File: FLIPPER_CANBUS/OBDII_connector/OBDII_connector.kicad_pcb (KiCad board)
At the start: 2 copper layers, 40 x 16.9 mm, 9 parts, among them J1 Conn_02x08_Counter_Clockwise, J2 Conn_01x02

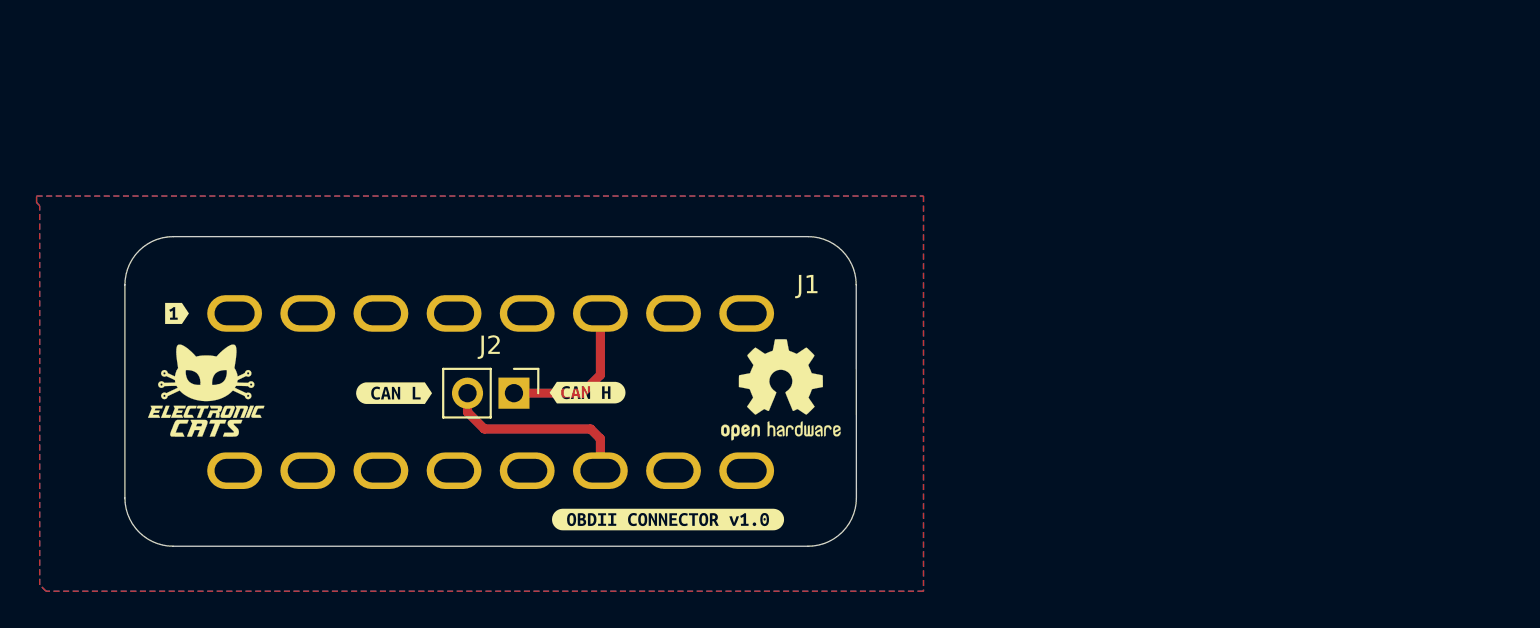
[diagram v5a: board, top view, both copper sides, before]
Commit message: feat: new dimensions added for OBDII connector
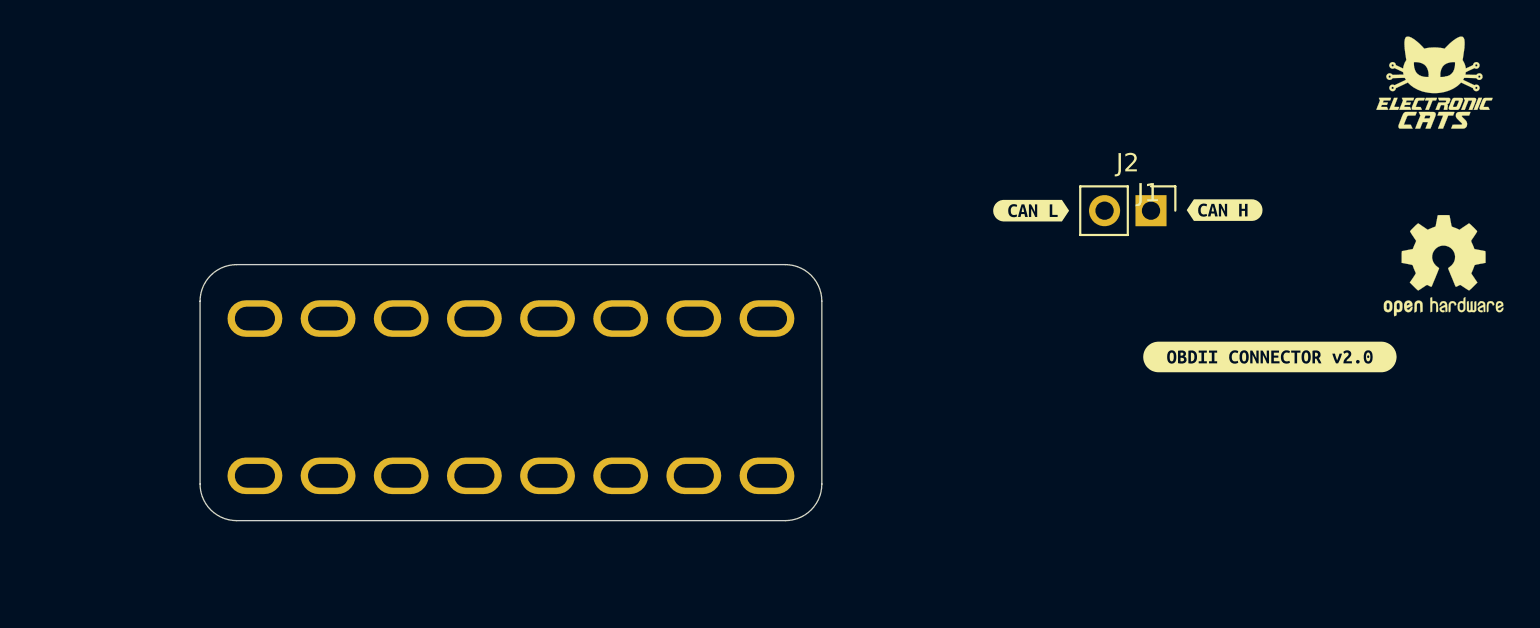
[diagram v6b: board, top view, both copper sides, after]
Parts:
- removed kibuzzard-66732750: G***, kibuzzard-66732750
- removed kibuzzard-667996B6: G***, kibuzzard-667996B6
- added kibuzzard-66AA5E2D: G***, kibuzzard-66AA5E2D, F.Cu at (157.5, 59.0)
- J1: footprint Case:OBD-II-Sparkfun -> Case:OBD-II-Sparkfun v2.0
- moved G*** 69.2 mm to (166.5, 44.0)
- moved G*** 36.9 mm to (166.8, 54.1)
- moved REF** 36.9 mm to (167.0, 54.0)
- moved kibuzzard-6646749E 36.2 mm to (155.0, 51.0)
- moved J2 36.2 mm to (151.0, 51.0)
- moved kibuzzard-66467618 36.2 mm to (144.4, 51.0)
- moved J1 1.14 mm to (116.0, 61.0)
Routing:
- net /CAN_L: track 10.7 -> 0.00 mm
- net /CAN_H: track 8.51 -> 0.00 mm
- removed copper zone on B.Cu, net GND
- removed copper zone on F.Cu, net GND
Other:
- board size 40 x 16.9 mm -> 34 x 14 mm

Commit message: feat: OBDII pcb design routed and labels got placed
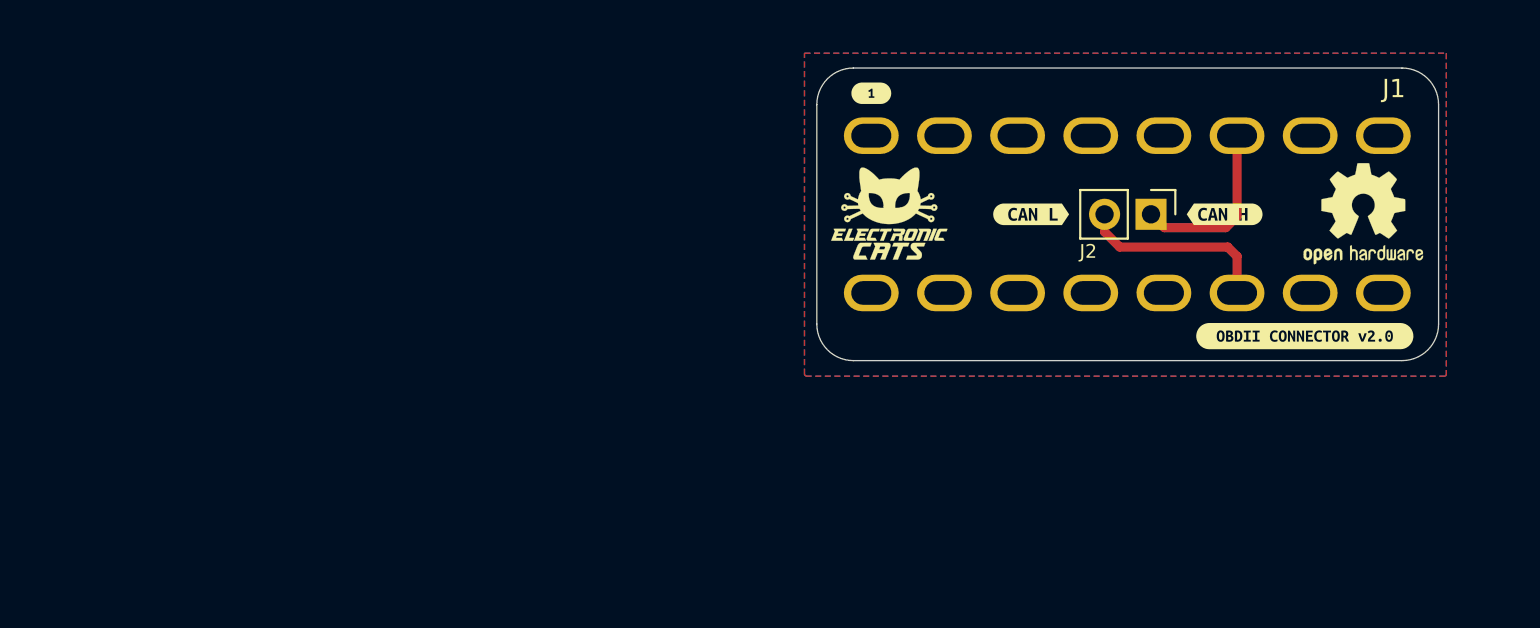
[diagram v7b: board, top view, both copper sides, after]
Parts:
- removed kibuzzard-66AA5E2D: G***, kibuzzard-66AA5E2D
- added kibuzzard-66AA65D6: G***, kibuzzard-66AA65D6, F.Cu at (135.7, 44.6)
- added kibuzzard-66AA65F0: G***, kibuzzard-66AA65F0, F.Cu at (159.4, 57.9)
- moved J1 35.2 mm to (149.7, 51.0)
- moved G*** 30.7 mm to (136.7, 51.2)
- moved G*** 5.23 mm to (162.4, 51.2)
- moved REF** 5.23 mm to (162.6, 51.2)
- moved kibuzzard-6646749E 0.23 mm to (155.0, 51.2)
- moved J2 0.20 mm to (151.0, 51.2)
- moved kibuzzard-66467618 0.20 mm to (144.4, 51.2)
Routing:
- net /CAN_L: track 0.00 -> 10.8 mm
- net /CAN_H: track 0.00 -> 9.68 mm
- added copper zone on B.Cu, net GND
- added copper zone on F.Cu, net GND
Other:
- board size 34 x 14 mm -> 34 x 16 mm
